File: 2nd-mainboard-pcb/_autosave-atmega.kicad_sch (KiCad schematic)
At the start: 31 parts, among them J10 FAN2, J11 FAN4, J2 Conn_02x03_Odd_Even, J3 T0, J4 T1, J5 T2, J6 T3, J8 FAN0, J9 FAN1, Q2 DTC143E, Q3 DTC143E, Q4 DTC143E, Q5 DTC143E, U1 ATmega328PB-A, Y1 ECS-160-18-4X-CKM

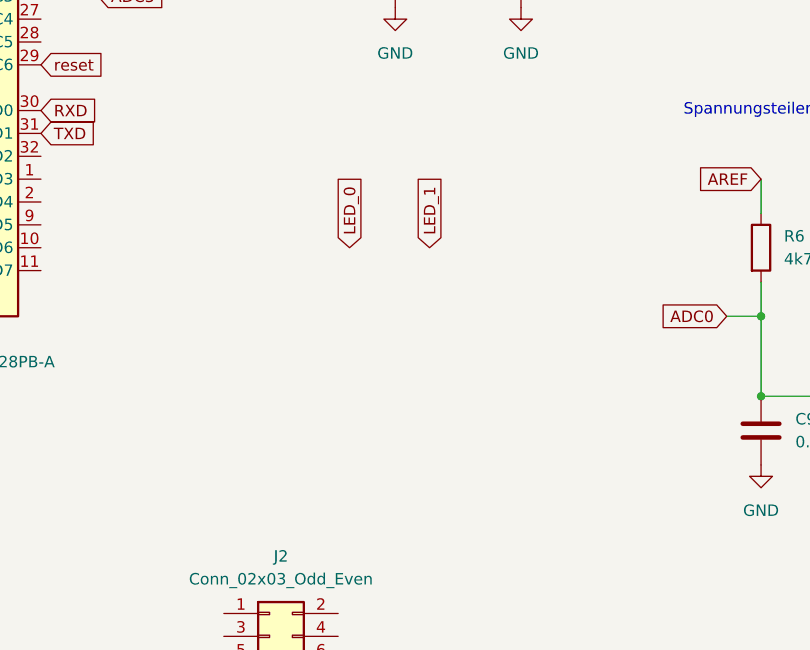
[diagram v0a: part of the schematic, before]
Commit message: added test point and documentation
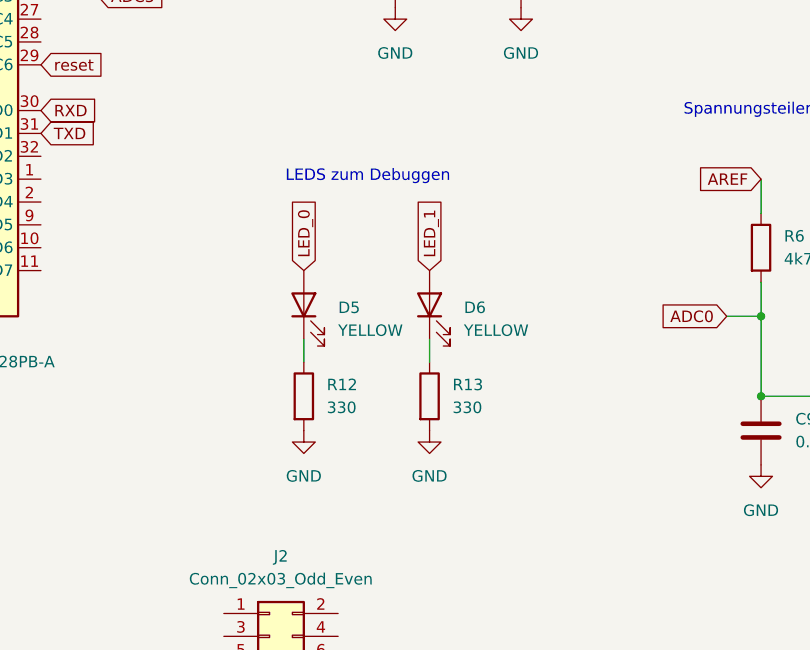
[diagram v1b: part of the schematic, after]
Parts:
- added D5, D6: YELLOW, LED_SMD:LED_0805_2012Metric, symbol Device:LED
- added R12, R13: 330, Resistor_SMD:R_0402_1005Metric, symbol Device:R
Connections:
- net GND: now also R12.2, R13.2
- net LED_0: now also D5.2 (A)
- net LED_1: now also D6.2 (A)
- new net: D6.1 (K), R13.1
- new net: D5.1 (K), R12.1
